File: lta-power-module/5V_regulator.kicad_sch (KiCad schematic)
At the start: 12 parts

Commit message: Small sheet cleanup.
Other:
- note added: "${REV_DATE}"
- note added: "${REV}"
- note added: "5V0 regulator"
- note added: "Power module 5V regulator (for driver logic)"
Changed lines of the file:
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@@
+    (effects (font (size 1.27 1.27)) (justify left bottom))
+  )
+  (text "Power module 5V regulator (for driver logic)" (at 184.785 173.99 0)
     (effects (font (size 1.27 1.27)) (justify left bottom))
   )
@@
     (effects (font (size 1.27 1.27)) (justify left bottom))
   )
+  (text "${REV}\n" (at 268.605 194.31 0)
+    (effects (font (size 1.27 1.27)) (justify left bottom))
+  )
   (text "Regulated 5V0 output" (at 176.53 65.405 0)
+    (effects (font (size 1.27 1.27)) (justify left bottom))
+  )
+  (text "5V0 regulator" (at 187.325 190.5 0)
     (effects (font (size 1.27 1.27)) (justify left bottom))
   )
@@
     (effects (font (size 1.27 1.27)) (justify left bottom))
   )
+  (text "${REV_DATE}" (at 207.01 194.31 0)
+    (effects (font (size 1.27 1.27)) (justify left bottom))
+  )

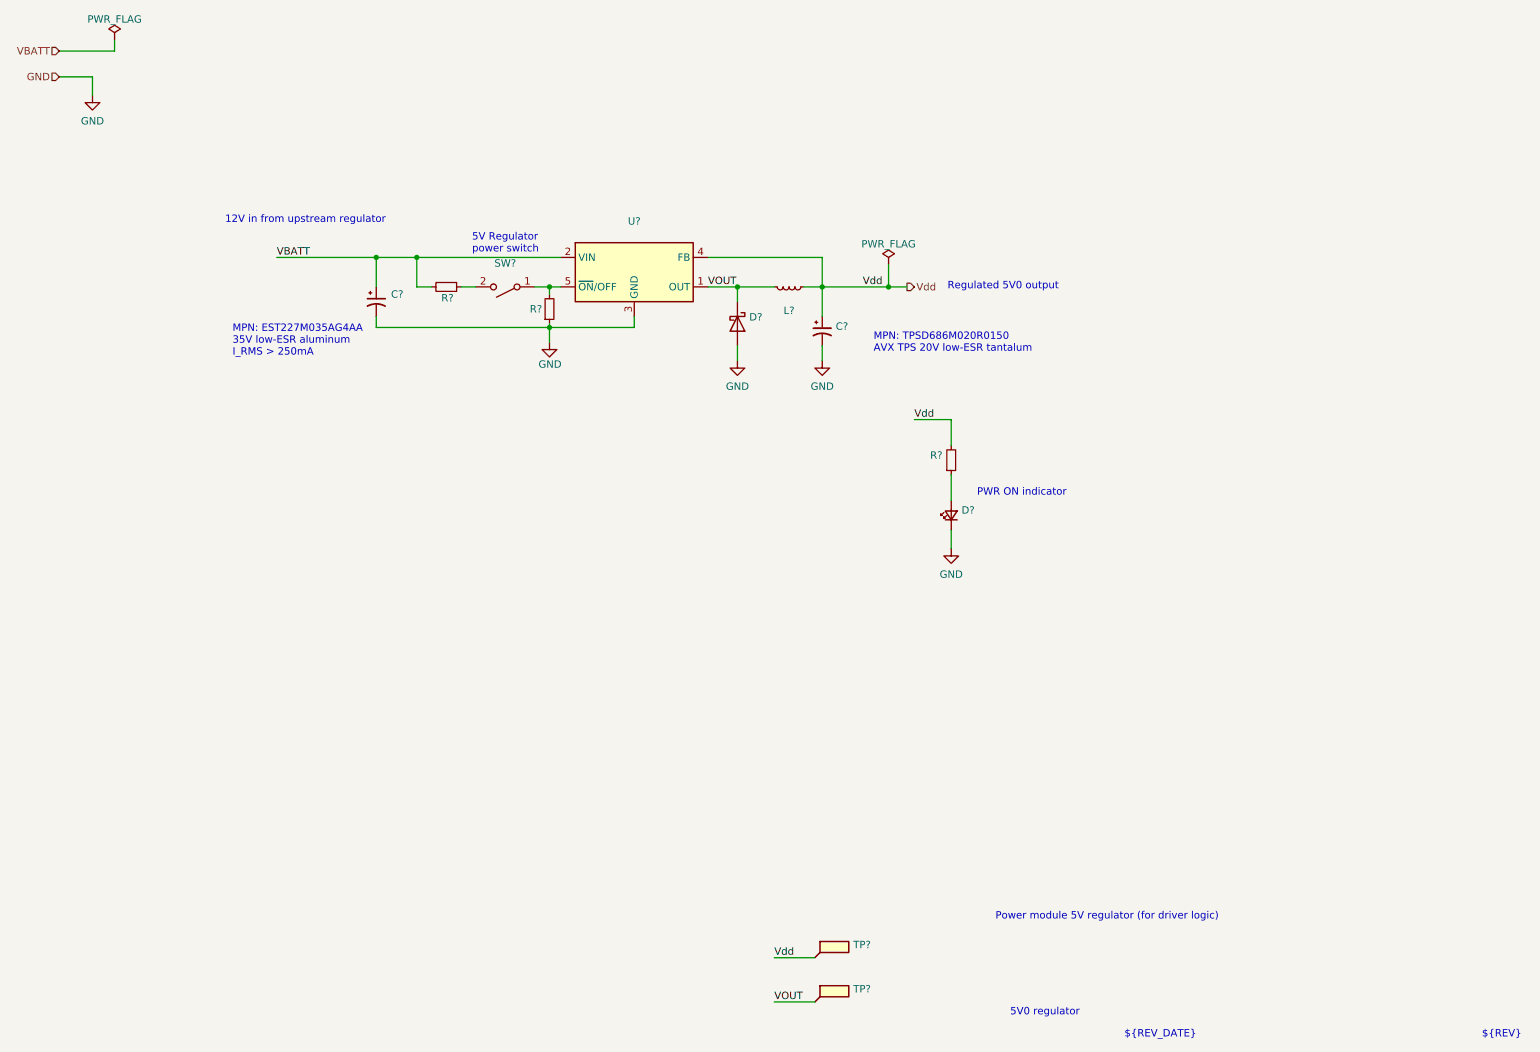
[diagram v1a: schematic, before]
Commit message: Add custom footprints for 12V regulator and power distribution bus.
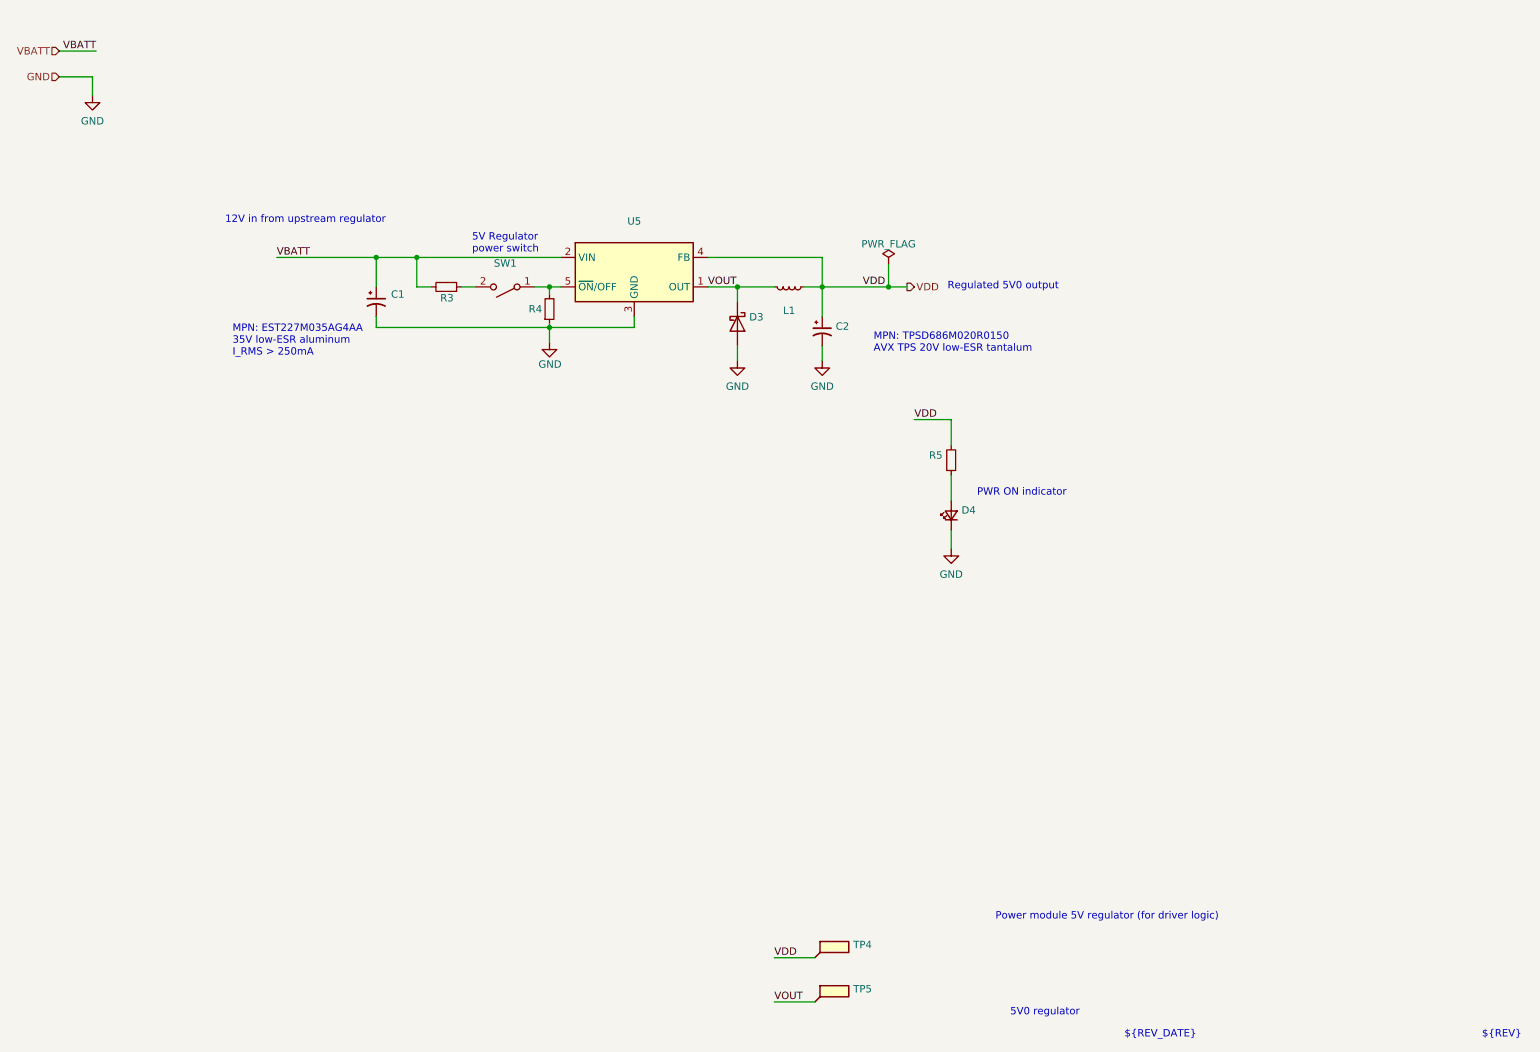
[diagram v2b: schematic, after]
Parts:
- D4: renamed from D?; Comment Vf=2.0V I_test=20mA red LED -> Vf=2.0V I_test=20mA red LED 5mm THT; MANUFACTURER (none) -> CreeLED; MPN (none) -> C5SMF-RJF-CT0W0BB1
- R3, R4: renamed from R?; Comment 10K 0603 resistor; +/-1%; 1/10W -> 10K THT resistor; +/-5%; 1/8W; MANUFACTURER YAEGO -> Stackpole; MPN RC0603FR-0710KL -> CF18JT10K0
- R5: renamed from R?; Comment 330R 0603 resistor; +/-1%; 1/10W -> 330R THT resistor; +/-5%; 1/8W; MANUFACTURER (none) -> Stackpole; MPN (none) -> CF18JT330R0
- gave numbers to parts that had none: 8
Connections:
- net Vdd renamed VDD

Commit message: Considerably more work on power module PCB.
* Slight reorganization of layout.
* Routed all traces.
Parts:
- R5: MPN CF18JT330R0 -> CF18JT330R
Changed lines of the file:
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@@
       (effects (font (size 1.27 1.27)) hide)
     )
-    (property "MPN" "CF18JT330R0" (id 6) (at 177.165 94.615 0)
+    (property "MPN" "CF18JT330R" (id 6) (at 177.165 94.615 0)
       (effects (font (size 1.27 1.27)) hide)
     )

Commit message: Add protoboard.
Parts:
- C1: SPN (none) -> 399-6615-ND; Supplier (none) -> DigiKey
- C2: SPN (none) -> 478-9217-1-ND; Supplier (none) -> DigiKey
- D3: SPN (none) -> SB530-E3/54GICT-ND; Supplier (none) -> DigiKey
- D4: SPN (none) -> C5SMF-RJF-CT0W0BB1-ND; Supplier (none) -> DigiKey
- L1: SPN (none) -> 535-13029-ND; Supplier (none) -> DigiKey
- R3, R4: SPN (none) -> CF18JT10K0CT-ND; Supplier (none) -> DigiKey
- R5: SPN (none) -> CF18JT330RCT-ND; Supplier (none) -> DigiKey
- SW1: SPN (none) -> 2223-DS01-254-S-01BE-ND; Supplier (none) -> DigiKey
- U5: SPN (none) -> LM2595T-5.0/NOPB-ND; Supplier (none) -> DigiKey
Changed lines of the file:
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@@
+      (effects (font (size 1.27 1.27)) hide)
+    )
+    (property "SPN" "2223-DS01-254-S-01BE-ND" (id 7) (at 100.33 64.77 0)
+      (effects (font (size 1.27 1.27)) hide)
+    )
+    (property "Supplier" "DigiKey" (id 8) (at 100.33 64.77 0)
       (effects (font (size 1.27 1.27)) hide)
     )
@@
       (effects (font (size 1.27 1.27)) hide)
     )
+    (property "SPN" "399-6615-ND" (id 7) (at 78.105 67.31 0)
+      (effects (font (size 1.27 1.27)) hide)
+    )
+    (property "Supplier" "DigiKey" (id 8) (at 78.105 67.31 0)
+      (effects (font (size 1.27 1.27)) hide)
+    )
     (pin "1")
     (pin "2")
@@
       (effects (font (size 1.27 1.27)) hide)
     )
+    (property "SPN" "478-9217-1-ND" (id 7) (at 154.94 72.39 0)
+      (effects (font (size 1.27 1.27)) hide)
+    )
+    (property "Supplier" "DigiKey" (id 8) (at 154.94 72.39 0)
+      (effects (font (size 1.27 1.27)) hide)
+    )
     (pin "1")
     (pin "2")
@@
     )
     (property "MPN" "CF18JT10K0" (id 6) (at 90.17 64.77 0)
+      (effects (font (size 1.27 1.27)) hide)
+    )
+    (property "SPN" "CF18JT10K0CT-ND" (id 7) (at 90.17 64.77 0)
+      (effects (font (size 1.27 1.27)) hide)
+    )
+    (property "Supplier" "DigiKey" (id 8) (at 90.17 64.77 0)
       (effects (font (size 1.27 1.27)) hide)
     )
@@
       (effects (font (size 1.27 1.27)) hide)
     )
+    (property "SPN" "LM2595T-5.0/NOPB-ND" (id 7) (at 122.555 62.23 0)
+      (effects (font (size 1.27 1.27)) hide)
+    )
+    (property "Supplier" "DigiKey" (id 8) (at 122.555 62.23 0)
+      (effects (font (size 1.27 1.27)) hide)
+    )
     (pin "1")
     (pin "2")
@@
       (effects (font (size 1.27 1.27)) hide)
     )
+    (property "SPN" "CF18JT10K0CT-ND" (id 7) (at 107.95 68.58 0)
+      (effects (font (size 1.27 1.27)) hide)
+    )
+    (property "Supplier" "DigiKey" (id 8) (at 107.95 68.58 0)
+      (effects (font (size 1.27 1.27)) hide)
+    )
     (pin "1")
     (pin "2")
@@
     )
     (property "Comment" "Vf=2.0V I_test=20mA red LED 5mm THT" (id 6) (at 177.165 104.14 90)
+      (effects (font (size 1.27 1.27)) hide)
+    )
+    (property "SPN" "C5SMF-RJF-CT0W0BB1-ND" (id 7) (at 177.165 104.14 0)
+      (effects (font (size 1.27 1.27)) hide)
+    )
+    (property "Supplier" "DigiKey" (id 8) (at 177.165 104.14 0)
       (effects (font (size 1.27 1.27)) hide)
     )
@@
       (effects (font (size 1.27 1.27)) hide)
     )
+    (property "SPN" "535-13029-ND" (id 7) (at 149.225 64.77 0)
+      (effects (font (size 1.27 1.27)) hide)
+    )
+    (property "Supplier" "DigiKey" (id 8) (at 149.225 64.77 0)
+      (effects (font (size 1.27 1.27)) hide)
+    )
     (pin "1")
     (pin "2")
@@
       (effects (font (size 1.27 1.27)) hide)
     )
+    (property "SPN" "CF18JT330RCT-ND" (id 7) (at 177.165 94.615 0)
+      (effects (font (size 1.27 1.27)) hide)
+    )
+    (property "Supplier" "DigiKey" (id 8) (at 177.165 94.615 0)
+      (effects (font (size 1.27 1.27)) hide)
+    )
     (pin "1")
     (pin "2")
@@
       (effects (font (size 1.27 1.27)) hide)
     )
+    (property "SPN" "SB530-E3/54GICT-ND" (id 7) (at 140.335 71.12 0)
+      (effects (font (size 1.27 1.27)) hide)
+    )
+    (property "Supplier" "DigiKey" (id 8) (at 140.335 71.12 0)
+      (effects (font (size 1.27 1.27)) hide)
+    )
